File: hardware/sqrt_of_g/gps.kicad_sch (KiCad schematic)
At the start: 5 parts, among them J26 SMA-J-P-H-ST-EM1, J27 SMA-J-P-H-ST-EM1, U8 Orion B16, U9 EP2W+

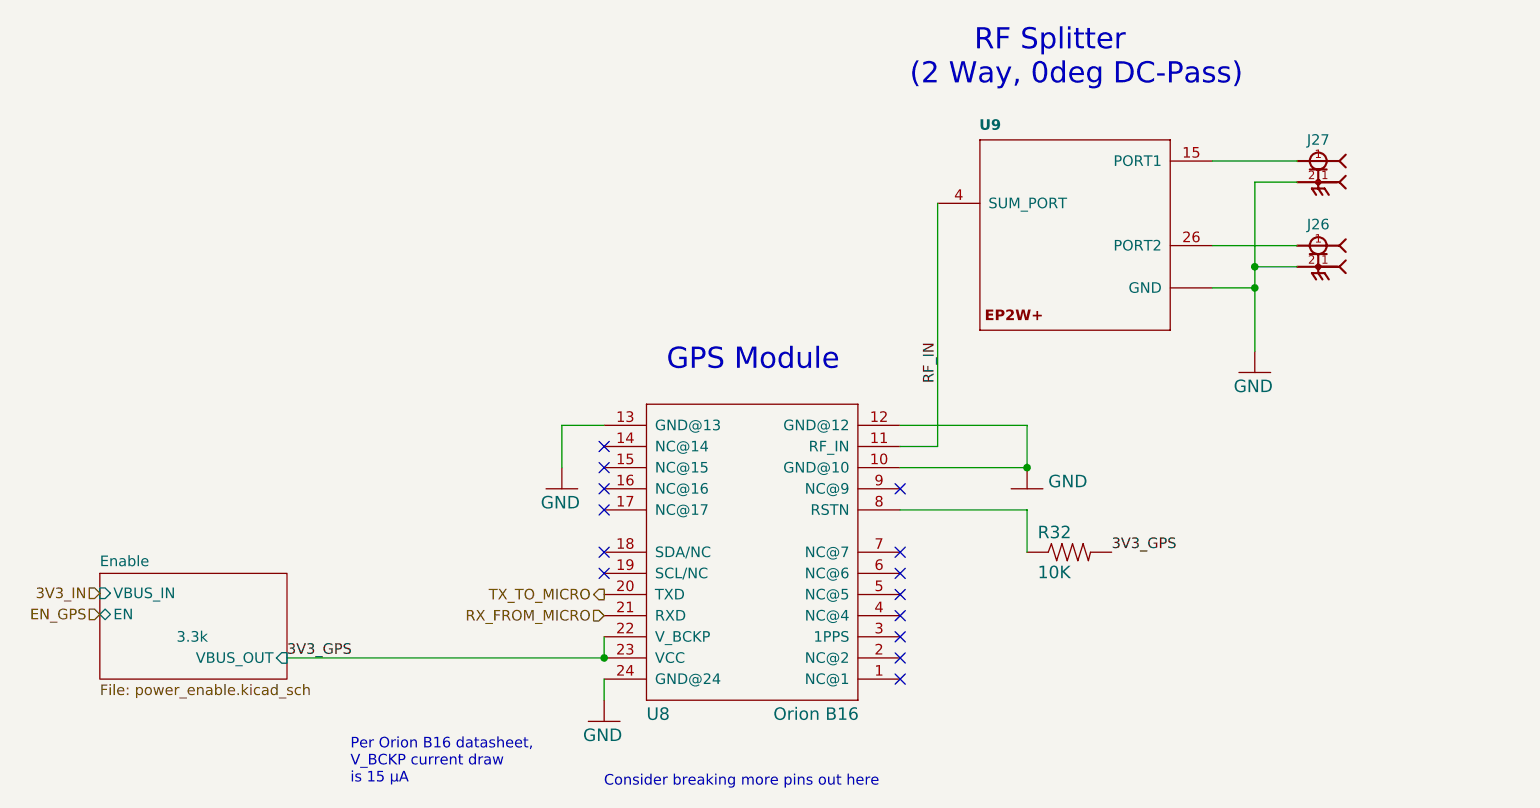
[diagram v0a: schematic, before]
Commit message: fix landing pattern
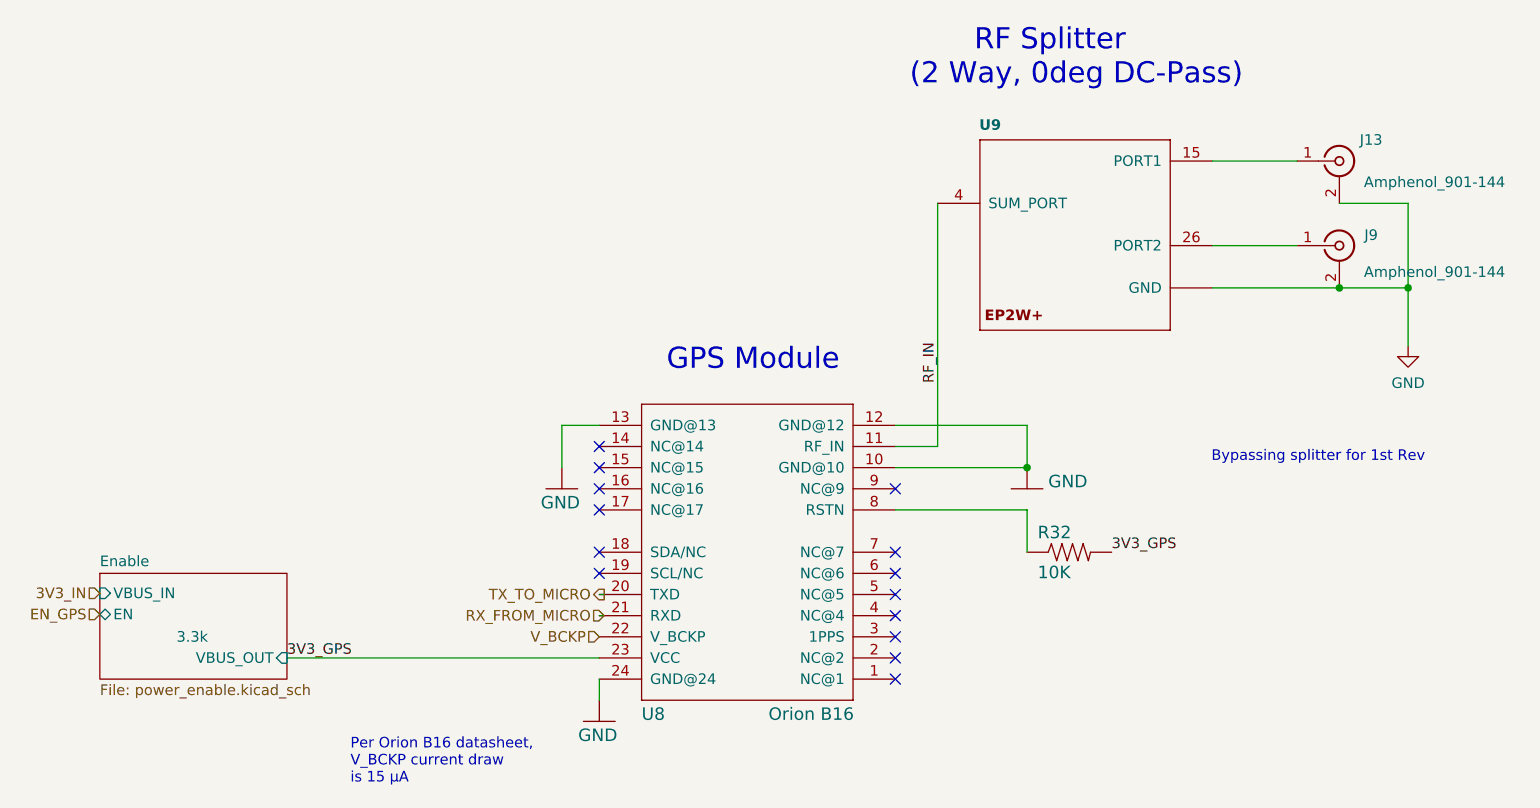
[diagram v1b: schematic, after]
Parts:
- removed J26, J27: SMA-J-P-H-ST-EM1, SMA-J-P-H-ST-EM1:SAMTEC_SMA-J-P-H-ST-EM1, symbol adcs:SMA-J-P-H-ST-EM1
- added J13, J9: Amphenol_901-144, Connector_Coaxial:SMA_Amphenol_901-144_Vertical, symbol Connector:Conn_Coaxial
- R32: footprint Resistor_SMD:R_0603_1608Metric -> Resistor_SMD:R_0402_1005Metric
- U8, U9: DNI DNI -> (none)
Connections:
- net 3V3_GPS: no longer U8.22 (V_BCKP)
- net GND: now also J13.2 (Ext), J9.2 (Ext)
- net at U9.26 (PORT2): now also J9.1 (In)
- net at U9.15 (PORT1): now also J13.1 (In)
- new net V_BCKP: U8.22 (V_BCKP)
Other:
- note added: "Bypassing splitter for 1st Rev"
- note removed: "Consider breaking more pins out here"
- title: (none) -> √g
- moved on the sheet: U8
